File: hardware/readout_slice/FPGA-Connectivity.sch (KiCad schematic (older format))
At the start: 24 parts

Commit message: auto push run at Wed Apr 14 09:17:01 EDT 2021
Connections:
- net FPGA_MOSI renamed D[00]
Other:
- note removed: "ADC does not go on this SPI bus"
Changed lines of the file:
@@
 $Descr A4 11693 8268
 encoding utf-8
-Sheet 12 15
+Sheet 11 14
 Title ""
 Date ""
@@
 NoConn ~ 2200 3850
 NoConn ~ 2200 3750
-Text HLabel 2300 3150 1    50   Input ~ 10
-Vcc_0
 Wire Wire Line
 	3150 4400 3150 4450
@@
 	4750 3850 4900 3850
 Connection ~ 4750 3850
-Text HLabel 4900 3450 2    50   Input ~ 10
-Vcc_0
 Wire Wire Line
 	4900 3450 4750 3450
 Connection ~ 4750 3450
-Text HLabel 3750 6750 1    50   Input ~ 10
-Vcc_0
 $Comp
 L power:GNDD #PWR?
@@
 Wire Wire Line
 	4700 3250 4900 3250
-Text HLabel 4900 3250 2    50   Input ~ 10
-Vcc_0
 Text Notes 4300 3050 0    50   ~ 0
 ug470 page 24
@@
 Wire Wire Line
 	2300 3250 2200 3250
-Text HLabel 3150 1750 1    50   Input ~ 10
-Vcc_0
 Text Notes 4150 1050 0    50   ~ 0
 Does power all sort out if vcc0 = 3v3
@@
 	6950 6300 6950 7800
 Wire Wire Line
-	3150 1900 3350 1900
-Wire Wire Line
-	3350 1900 3350 1750
-Connection ~ 3150 1900
-Wire Wire Line
-	3150 1900 3150 1750
-$Comp
-L power:+3V3 #PWR?
-U 1 1 6070E178
-P 3350 1750
-F 0 "#PWR?" H 3350 1600 50  0001 C CNN
-F 1 "+3V3" H 3350 1900 50  0000 C CNN
-F 2 "" H 3350 1750 50  0001 C CNN
-F 3 "" H 3350 1750 50  0001 C CNN
-	1    3350 1750
-	1    0    0    -1
-$EndComp
-Wire Wire Line
 	4300 3050 4900 3050
-Text HLabel 4900 3050 2    50   Input ~ 10
-Vcc_0
 $Comp
 L readout:XC7A35T-1FGG484 U?
@@
 	9450 1650 9450 1550
 Connection ~ 9450 1650
-Text HLabel 9450 1550 1    50   Input ~ 10
-Vcc_0
 Wire Wire Line
 	9450 1650 9450 2100
@@
 Text Notes 6400 2650 0    50   ~ 10
 128Mb
-$Comp
-L power:+3V3 #PWR?
-U 1 1 6094400A
-P 6200 2000
-F 0 "#PWR?" H 6200 1850 50  0001 C CNN
-F 1 "+3V3" H 6200 2150 50  0000 C CNN
-F 2 "" H 6200 2000 50  0001 C CNN
-F 3 "" H 6200 2000 50  0001 C CNN
-	1    6200 2000
-	1    0    0    -1
-$EndComp
 Wire Wire Line
 	5300 1700 5500 1700
@@
 Wire Wire Line
 	5700 1700 5700 1800
-Wire Wire Line
-	5200 1700 5300 1700
-Text HLabel 5200 1700 0    50   Input ~ 10
-Vcc_0
-Text Notes 5050 1600 0    50   ~ 0
+Text Notes 4000 1850 0    50   ~ 0
 Look at xapp586 page 7\nshould S, W, HOLD all be ‘nots’
 Wire Wire Line
@@
 NoConn ~ 4300 2400
 NoConn ~ 4300 2500
-Text HLabel 7100 2300 0    50   Input ~ 0
-FPGA_MOSI
 Text HLabel 5000 2700 2    50   Input ~ 0
 FPGA_CCLK_0
@@
 Wire Wire Line
 	4300 2800 4900 2800
-Text Notes 7250 1150 0    157  ~ 31
-ADC does not go on this SPI bus
+$Comp
+L power:+3V3 #PWR?
+U 1 1 60894F31
+P 9450 1550
+F 0 "#PWR?" H 9450 1400 50  0001 C CNN
+F 1 "+3V3" H 9450 1700 50  0000 C CNB
+F 2 "" H 9450 1550 50  0001 C CNN
+F 3 "" H 9450 1550 50  0001 C CNN
+	1    9450 1550
+	1    0    0    -1
+$EndComp
+$Comp
+L power:+3V3 #PWR?
+U 1 1 6089A00F
+P 5300 1600
+F 0 "#PWR?" H 5300 1450 50  0001 C CNN
+F 1 "+3V3" H 5300 1750 50  0000 C CNB
+F 2 "" H 5300 1600 50  0001 C CNN
+F 3 "" H 5300 1600 50  0001 C CNN
+	1    5300 1600
+	1    0    0    -1
+$EndComp
+Wire Wire Line
+	5300 1700 5300 1600
+$Comp
+L power:+3V3 #PWR?
+U 1 1 6089FEE0
+P 6200 2000
+F 0 "#PWR?" H 6200 1850 50  0001 C CNN
+F 1 "+3V3" H 6200 2150 50  0000 C CNB
+F 2 "" H 6200 2000 50  0001 C CNN
+F 3 "" H 6200 2000 50  0001 C CNN
+	1    6200 2000
+	1    0    0    -1
+$EndComp
+$Comp
+L power:+3V3 #PWR?
+U 1 1 608A04F6
+P 3150 1900
+F 0 "#PWR?" H 3150 1750 50  0001 C CNN
+F 1 "+3V3" H 3150 2050 50  0000 C CNB
+F 2 "" H 3150 1900 50  0001 C CNN
+F 3 "" H 3150 1900 50  0001 C CNN
+	1    3150 1900
+	1    0    0    -1
+$EndComp
+$Comp
+L power:+3V3 #PWR?
+U 1 1 608A0A7D
+P 2300 3150
+F 0 "#PWR?" H 2300 3000 50  0001 C CNN
+F 1 "+3V3" H 2300 3300 50  0000 C CNB
+F 2 "" H 2300 3150 50  0001 C CNN
+F 3 "" H 2300 3150 50  0001 C CNN
+	1    2300 3150
+	1    0    0    -1
+$EndComp
+$Comp
+L power:+3V3 #PWR?
+U 1 1 608A330A
+P 4900 3450
+F 0 "#PWR?" H 4900 3300 50  0001 C CNN
+F 1 "+3V3" V 4900 3650 50  0000 C CNB
+F 2 "" H 4900 3450 50  0001 C CNN
+F 3 "" H 4900 3450 50  0001 C CNN
+	1    4900 3450
+	0    1    1    0
+$EndComp
+$Comp
+L power:+3V3 #PWR?
+U 1 1 608A5046
+P 4900 3250
+F 0 "#PWR?" H 4900 3100 50  0001 C CNN
+F 1 "+3V3" V 4900 3450 50  0000 C CNB
+F 2 "" H 4900 3250 50  0001 C CNN
+F 3 "" H 4900 3250 50  0001 C CNN
+	1    4900 3250
+	0    1    1    0
+$EndComp
+$Comp
+L power:+3V3 #PWR?
+U 1 1 608A52D9
+P 4900 3050
+F 0 "#PWR?" H 4900 2900 50  0001 C CNN
+F 1 "+3V3" V 4900 3250 50  0000 C CNB
+F 2 "" H 4900 3050 50  0001 C CNN
+F 3 "" H 4900 3050 50  0001 C CNN
+	1    4900 3050
+	0    1    1    0
+$EndComp
+$Comp
+L power:+3V3 #PWR?
+U 1 1 608A795D
+P 3750 6750
+F 0 "#PWR?" H 3750 6600 50  0001 C CNN
+F 1 "+3V3" H 3750 6900 50  0000 C CNB
+F 2 "" H 3750 6750 50  0001 C CNN
+F 3 "" H 3750 6750 50  0001 C CNN
+	1    3750 6750
+	1    0    0    -1
+$EndComp
 $EndSCHEMATC

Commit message: auto push run at Wed Apr 21 10:59:57 EDT 2021
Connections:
- net FPGA_CCLK_0: no longer names the net of U?.6 (C), U?.L12 (CCLK_0)
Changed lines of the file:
@@
 $Descr A4 11693 8268
 encoding utf-8
-Sheet 11 14
+Sheet 14 14
 Title ""
 Date ""
@@
 	1    0    0    -1
 $EndComp
-Wire Wire Line
-	5800 2800 4900 2800
 Text Label 7100 2400 0    50   ~ 0
 DIN\D[01]
@@
 NoConn ~ 4300 2400
 NoConn ~ 4300 2500
-Text HLabel 5000 2700 2    50   Input ~ 0
-FPGA_CCLK_0
-Wire Wire Line
-	4900 2800 4900 2700
-Wire Wire Line
-	4900 2700 5000 2700
-Connection ~ 4900 2800
-Wire Wire Line
-	4300 2800 4900 2800
 $Comp
 L power:+3V3 #PWR?
@@
 	1    0    0    -1
 $EndComp
+Wire Wire Line
+	4300 2800 5800 2800
 $EndSCHEMATC

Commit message: auto push run at Wed Apr 21 11:14:23 EDT 2021
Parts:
- added U?: XC7A35T-1FGG484, symbol readout:XC7A35T-1FGG484
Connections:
- no-connect marks 22 -> 43
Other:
- moved on the sheet: C?, J?, R?, U?, U?B, U?D

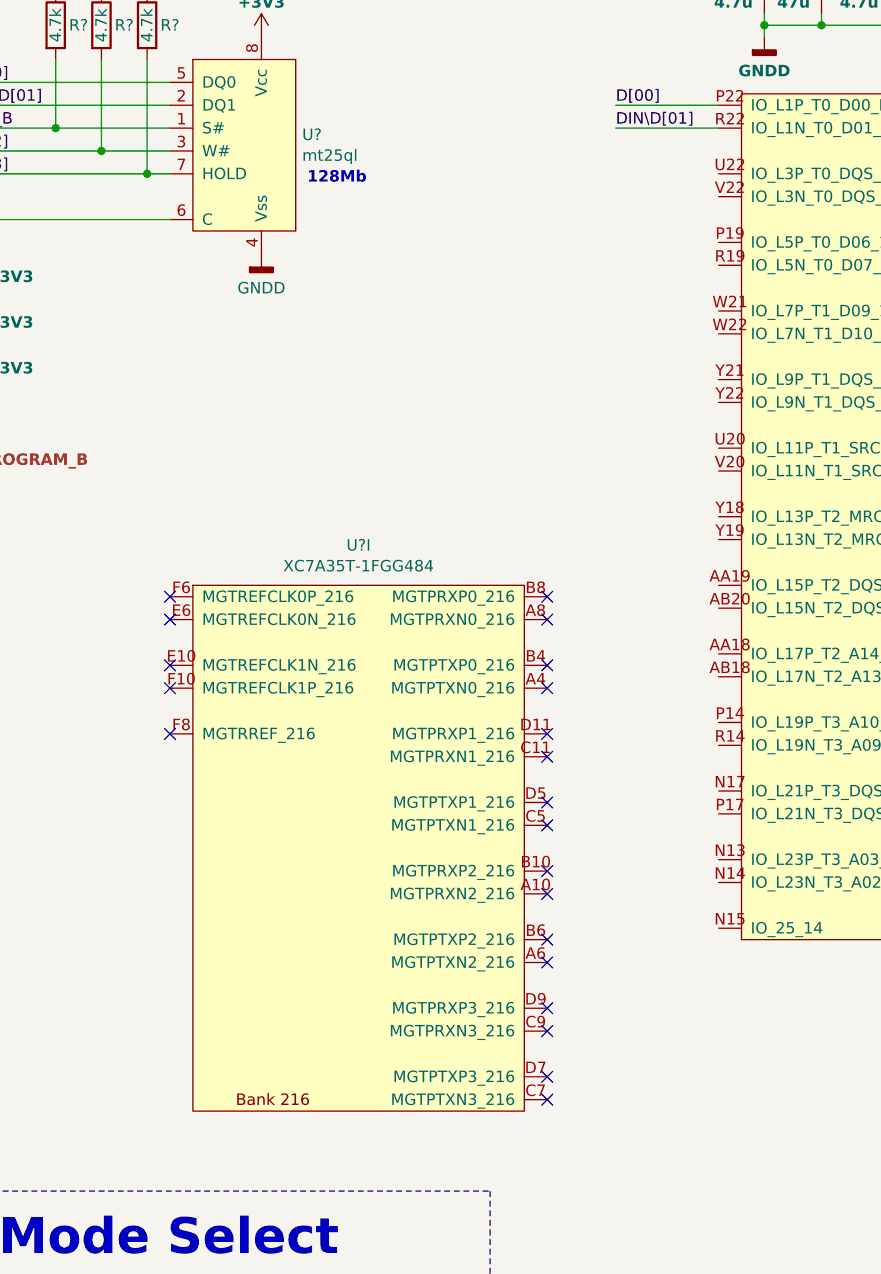
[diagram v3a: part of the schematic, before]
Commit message: removed zx2, added sfp for serdes from dan's vice board
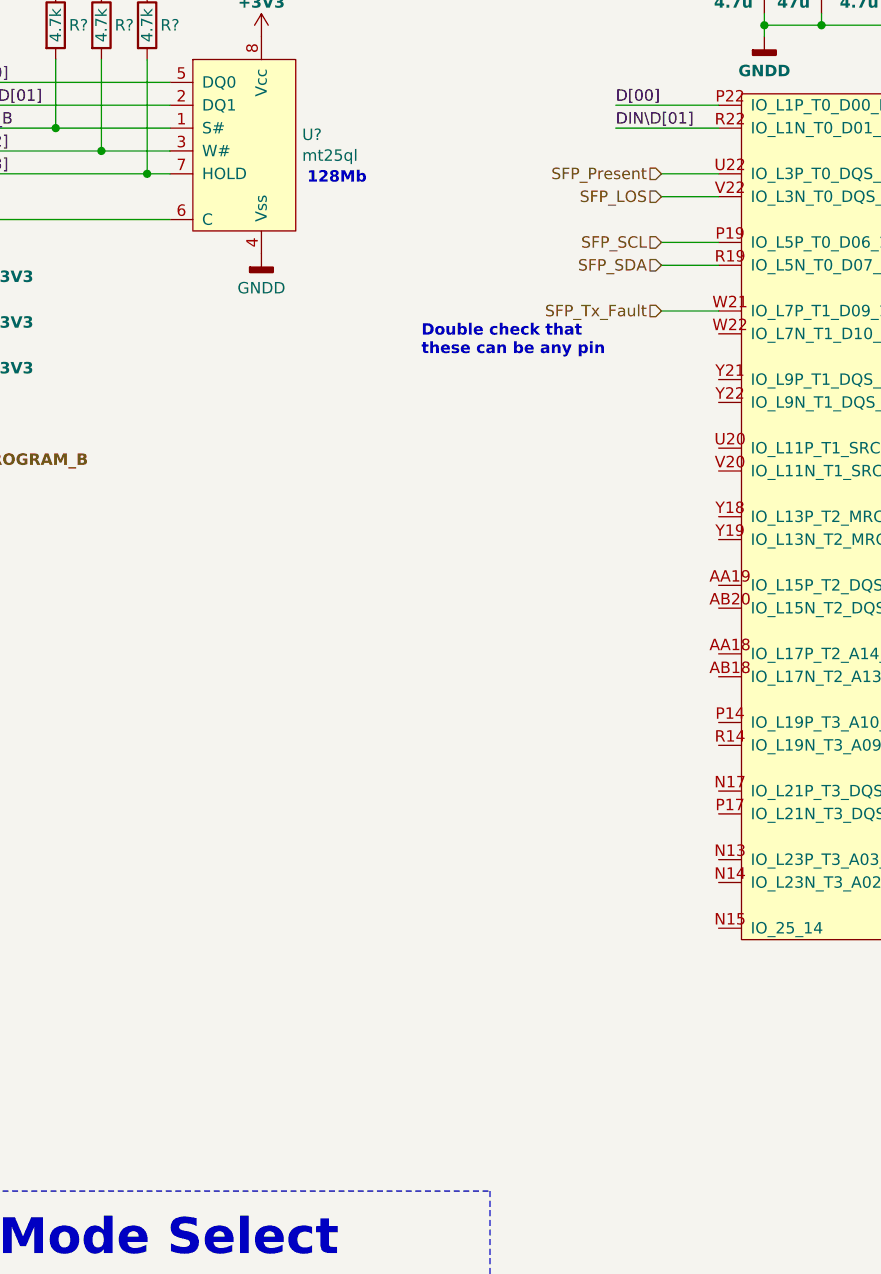
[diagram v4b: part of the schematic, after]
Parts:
- removed U?: XC7A35T-1FGG484, symbol readout:XC7A35T-1FGG484
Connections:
- net SFP_SCL: now reaches U?.P19 (IO_L5P_T0_D06_14)
- net SFP_SDA: now reaches U?.R19 (IO_L5N_T0_D07_14)
- net SFP_Present: now reaches U?.U22 (IO_L3P_T0_DQS_PUDC_B_14)
- net SFP_LOS: now reaches U?.V22 (IO_L3N_T0_DQS_EMCCLK_14)
- net SFP_Tx_Fault: now reaches U?.W21 (IO_L7P_T1_D09_14)
- no-connect marks 43 -> 22
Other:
- note added: "Double check that\nthese can be any pin"
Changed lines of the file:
@@
 $Descr A4 11693 8268
 encoding utf-8
-Sheet 12 14
+Sheet 8 11
 Title ""
 Date ""
@@
 Wire Wire Line
 	4050 2050 5550 2050
-$Comp
-L readout:XC7A35T-1FGG484 U?
-U 9 1 639D3E9A
-P 6450 3650
-AR Path="/605605C8/639D3E9A" Ref="U?"  Part="9"
-AR Path="/639D3E9A" Ref="U?"  Part="9"
-AR Path="/608F6DFA/639D3E9A" Ref="U?"  Part="9"
-F 0 "U?" H 6375 3825 50  0000 C CNN
-F 1 "XC7A35T-1FGG484" H 6375 3734 50  0000 C CNN
-F 2 "" H 5350 3800 50  0001 C CNN
-F 3 "" H 5350 3800 50  0001 C CNN
-	9    6450 3650
-	1    0    0    -1
-$EndComp
-NoConn ~ 5550 4300
-NoConn ~ 5550 4100
-NoConn ~ 5550 4000
-NoConn ~ 5550 3800
-NoConn ~ 5550 3700
-NoConn ~ 7200 3700
-NoConn ~ 7200 3800
-NoConn ~ 7200 4000
-NoConn ~ 7200 4100
-NoConn ~ 7200 4300
-NoConn ~ 7200 4400
-NoConn ~ 7200 4600
-NoConn ~ 7200 4700
-NoConn ~ 7200 4900
-NoConn ~ 7200 5000
-NoConn ~ 7200 5200
-NoConn ~ 7200 5300
-NoConn ~ 7200 5500
-NoConn ~ 7200 5600
-NoConn ~ 7200 5800
-NoConn ~ 7200 5900
+Text HLabel 7700 1850 0    50   Input ~ 0
+SFP_Present
+Text HLabel 7700 1950 0    50   Input ~ 0
+SFP_LOS
+Text HLabel 7700 2450 0    50   Input ~ 0
+SFP_Tx_Fault
+Text HLabel 7700 2150 0    50   Input ~ 0
+SFP_SCL
+Text HLabel 7700 2250 0    50   Input ~ 0
+SFP_SDA
+Wire Wire Line
+	7950 1850 7700 1850
+Wire Wire Line
+	7700 1950 7950 1950
+Wire Wire Line
+	7950 2150 7700 2150
+Wire Wire Line
+	7700 2250 7950 2250
+Wire Wire Line
+	7950 2450 7700 2450
+Text Notes 6650 2650 0    50   ~ 10
+Double check that\nthese can be any pin
 $EndSCHEMATC

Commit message: auto push run at Wed Apr 28 10:36:58 EDT 2021
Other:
- note added: "Double check that\nSFP can be any pin"
- note removed: "Double check that\nthese can be any pin"
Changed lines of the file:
@@
 	7950 2450 7700 2450
 Text Notes 6650 2650 0    50   ~ 10
-Double check that\nthese can be any pin
+Double check that\nSFP can be any pin
 $EndSCHEMATC

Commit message: auto push run at Wed Apr 28 10:51:45 EDT 2021
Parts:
- added U? (x8): Vcc0, symbol readout:Vcc0
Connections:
- net +3V3: no longer C?.1, C?.1, C?.1, C?.1, C?.1, C?.1, C?.1, C?.1, J?.1 (Pin_1), J?.1 (Pin_1), J?.1 (Pin_1), R?.1, R?.1, R?.1, R?.1, R?.1, R?.2, U?.8 (Vcc), U?.F12 (VCCO_0), U?.M14 (VCCO_14), U?.P18 (VCCO_14), U?.R15 (VCCO_14), U?.T12 (VCCO_0), U?.T22 (VCCO_14), U?.U19 (VCCO_14), U?.U8 (CFGBVS_0), U?.Y20 (VCCO_14)
- new net VCC: C?.1, C?.1, C?.1, C?.1, C?.1, C?.1, C?.1, C?.1, J?.1 (Pin_1), J?.1 (Pin_1), J?.1 (Pin_1), R?.1, R?.1, R?.1, R?.1, R?.1, R?.2, U?.1 (VCC), U?.1 (VCC), U?.1 (VCC), U?.1 (VCC), U?.1 (VCC), U?.1 (VCC), U?.1 (VCC), U?.1 (VCC), U?.8 (Vcc), U?.F12 (VCCO_0), U?.M14 (VCCO_14), U?.P18 (VCCO_14), U?.R15 (VCCO_14), U?.T12 (VCCO_0), U?.T22 (VCCO_14), U?.U19 (VCCO_14), U?.U8 (CFGBVS_0), U?.Y20 (VCCO_14)
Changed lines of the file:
@@
 $Descr A4 11693 8268
 encoding utf-8
-Sheet 8 11
+Sheet 7 11
 Title ""
 Date ""
@@
 NoConn ~ 4050 1650
 NoConn ~ 4050 1750
-$Comp
-L power:+3V3 #PWR?
-U 1 1 60894F31
-P 9850 800
-F 0 "#PWR?" H 9850 650 50  0001 C CNN
-F 1 "+3V3" H 9850 950 50  0000 C CNB
-F 2 "" H 9850 800 50  0001 C CNN
-F 3 "" H 9850 800 50  0001 C CNN
-	1    9850 800
-	1    0    0    -1
-$EndComp
-$Comp
-L power:+3V3 #PWR?
-U 1 1 6089A00F
-P 5050 850
-F 0 "#PWR?" H 5050 700 50  0001 C CNN
-F 1 "+3V3" H 5050 1000 50  0000 C CNB
-F 2 "" H 5050 850 50  0001 C CNN
-F 3 "" H 5050 850 50  0001 C CNN
-	1    5050 850
-	1    0    0    -1
-$EndComp
 Wire Wire Line
 	5050 950  5050 850
-$Comp
-L power:+3V3 #PWR?
-U 1 1 6089FEE0
-P 5950 1250
-F 0 "#PWR?" H 5950 1100 50  0001 C CNN
-F 1 "+3V3" H 5950 1400 50  0000 C CNB
-F 2 "" H 5950 1250 50  0001 C CNN
-F 3 "" H 5950 1250 50  0001 C CNN
-	1    5950 1250
-	1    0    0    -1
-$EndComp
-$Comp
-L power:+3V3 #PWR?
-U 1 1 608A04F6
-P 2900 1150
-F 0 "#PWR?" H 2900 1000 50  0001 C CNN
-F 1 "+3V3" H 2900 1300 50  0000 C CNB
-F 2 "" H 2900 1150 50  0001 C CNN
-F 3 "" H 2900 1150 50  0001 C CNN
-	1    2900 1150
-	1    0    0    -1
-$EndComp
 $Comp
 L power:+3V3 #PWR?
@@
 F 3 "" H 2050 2400 50  0001 C CNN
 	1    2050 2400
-	1    0    0    -1
-$EndComp
-$Comp
-L power:+3V3 #PWR?
-U 1 1 608A330A
-P 4650 2700
-F 0 "#PWR?" H 4650 2550 50  0001 C CNN
-F 1 "+3V3" V 4650 2900 50  0000 C CNB
-F 2 "" H 4650 2700 50  0001 C CNN
-F 3 "" H 4650 2700 50  0001 C CNN
-	1    4650 2700
-	0    1    1    0
-$EndComp
-$Comp
-L power:+3V3 #PWR?
-U 1 1 608A5046
-P 4650 2500
-F 0 "#PWR?" H 4650 2350 50  0001 C CNN
-F 1 "+3V3" V 4650 2700 50  0000 C CNB
-F 2 "" H 4650 2500 50  0001 C CNN
-F 3 "" H 4650 2500 50  0001 C CNN
-	1    4650 2500
-	0    1    1    0
-$EndComp
-$Comp
-L power:+3V3 #PWR?
-U 1 1 608A52D9
-P 4650 2300
-F 0 "#PWR?" H 4650 2150 50  0001 C CNN
-F 1 "+3V3" V 4650 2500 50  0000 C CNB
-F 2 "" H 4650 2300 50  0001 C CNN
-F 3 "" H 4650 2300 50  0001 C CNN
-	1    4650 2300
-	0    1    1    0
-$EndComp
-$Comp
-L power:+3V3 #PWR?
-U 1 1 608A795D
-P 3750 6750
-F 0 "#PWR?" H 3750 6600 50  0001 C CNN
-F 1 "+3V3" H 3750 6900 50  0000 C CNB
-F 2 "" H 3750 6750 50  0001 C CNN
-F 3 "" H 3750 6750 50  0001 C CNN
-	1    3750 6750
 	1    0    0    -1
 $EndComp
@@
 Text Notes 6650 2650 0    50   ~ 10
 Double check that\nSFP can be any pin
+$Comp
+L readout:Vcc0 U?
+U 1 1 62C96DDE
+P 2900 1050
+F 0 "U?" H 2900 1050 79  0001 C CNN
+F 1 "Vcc0" H 2800 1100 47  0000 L CNB
+F 2 "" H 2900 1050 79  0001 C CNN
+F 3 "" H 2900 1050 79  0001 C CNN
+	1    2900 1050
+	1    0    0    -1
+$EndComp
+$Comp
+L readout:Vcc0 U?
+U 1 1 62C97174
+P 5050 750
+F 0 "U?" H 5050 750 79  0001 C CNN
+F 1 "Vcc0" H 4950 800 47  0000 L CNB
+F 2 "" H 5050 750 79  0001 C CNN
+F 3 "" H 5050 750 79  0001 C CNN
+	1    5050 750
+	1    0    0    -1
+$EndComp
+$Comp
+L readout:Vcc0 U?
+U 1 1 62C98336
+P 5950 1150
+F 0 "U?" H 5950 1150 79  0001 C CNN
+F 1 "Vcc0" H 5850 1200 47  0000 L CNB
+F 2 "" H 5950 1150 79  0001 C CNN
+F 3 "" H 5950 1150 79  0001 C CNN
+	1    5950 1150
+	1    0    0    -1
+$EndComp
+$Comp
+L readout:Vcc0 U?
+U 1 1 62C9F6A2
+P 9850 700
+F 0 "U?" H 9850 700 79  0001 C CNN
+F 1 "Vcc0" H 9750 750 47  0000 L CNB
+F 2 "" H 9850 700 79  0001 C CNN
+F 3 "" H 9850 700 79  0001 C CNN
+	1    9850 700
+	1    0    0    -1
+$EndComp
+$Comp
+L readout:Vcc0 U?
+U 1 1 62CAB47F
+P 4750 2300
+F 0 "U?" H 4750 2300 79  0001 C CNN
+F 1 "Vcc0" V 4700 2300 47  0000 L CNB
+F 2 "" H 4750 2300 79  0001 C CNN
+F 3 "" H 4750 2300 79  0001 C CNN
+	1    4750 2300
+	0    1    1    0
+$EndComp
+$Comp
+L readout:Vcc0 U?
+U 1 1 62CBA584
+P 4750 2500
+F 0 "U?" H 4750 2500 79  0001 C CNN
+F 1 "Vcc0" V 4700 2500 47  0000 L CNB
+F 2 "" H 4750 2500 79  0001 C CNN
+F 3 "" H 4750 2500 79  0001 C CNN
+	1    4750 2500
+	0    1    1    0
+$EndComp
+$Comp
+L readout:Vcc0 U?
+U 1 1 62CBA7D3
+P 4750 2700
+F 0 "U?" H 4750 2700 79  0001 C CNN
+F 1 "Vcc0" V 4700 2700 47  0000 L CNB
+F 2 "" H 4750 2700 79  0001 C CNN
+F 3 "" H 4750 2700 79  0001 C CNN
+	1    4750 2700
+	0    1    1    0
+$EndComp
+$Comp
+L readout:Vcc0 U?
+U 1 1 62CBD301
+P 3750 6650
+F 0 "U?" H 3750 6650 79  0001 C CNN
+F 1 "Vcc0" H 3650 6700 47  0000 L CNB
+F 2 "" H 3750 6650 79  0001 C CNN
+F 3 "" H 3750 6650 79  0001 C CNN
+	1    3750 6650
+	1    0    0    -1
+$EndComp
 $EndSCHEMATC
